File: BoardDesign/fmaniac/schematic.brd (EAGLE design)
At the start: 20 x 39 mm, 20 parts, among them U1 ATMEGA168MLF, X1 STEREOJACK

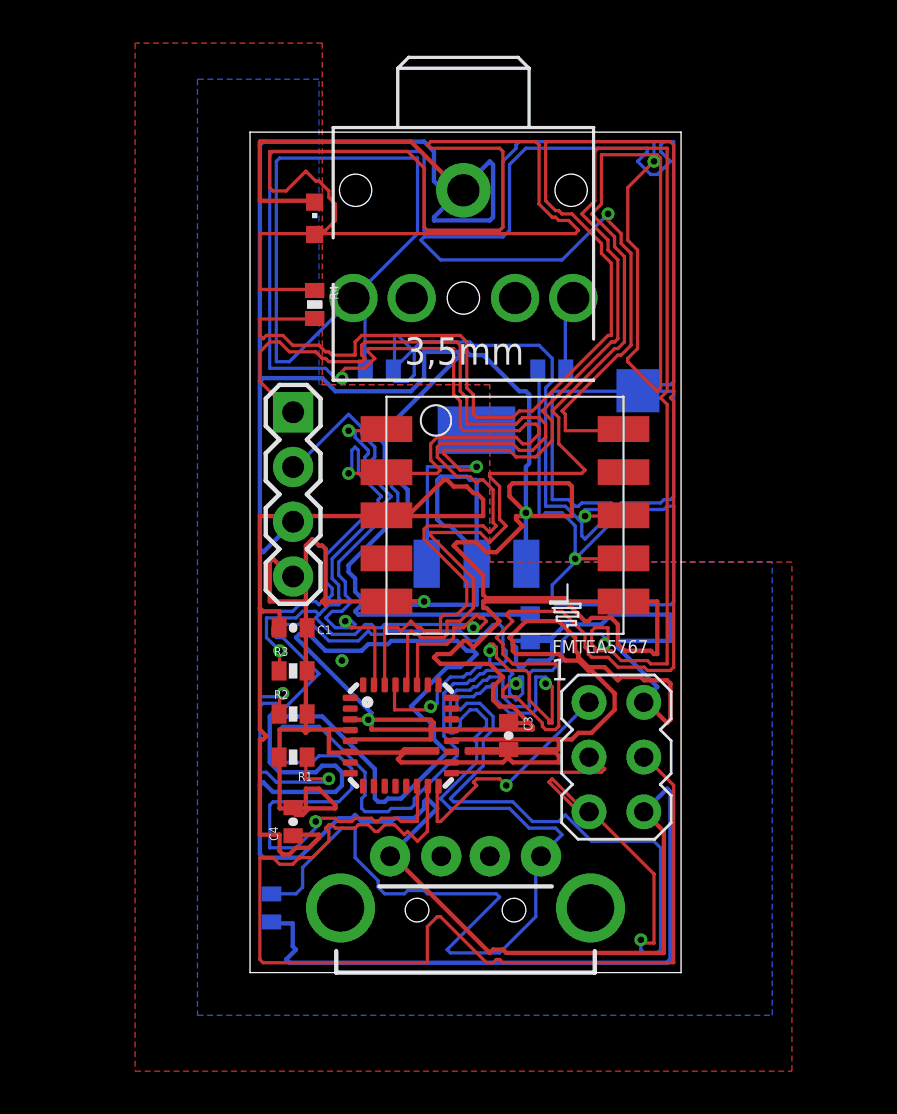
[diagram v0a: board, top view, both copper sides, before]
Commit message: Normal Push, Interrupt Button Added.
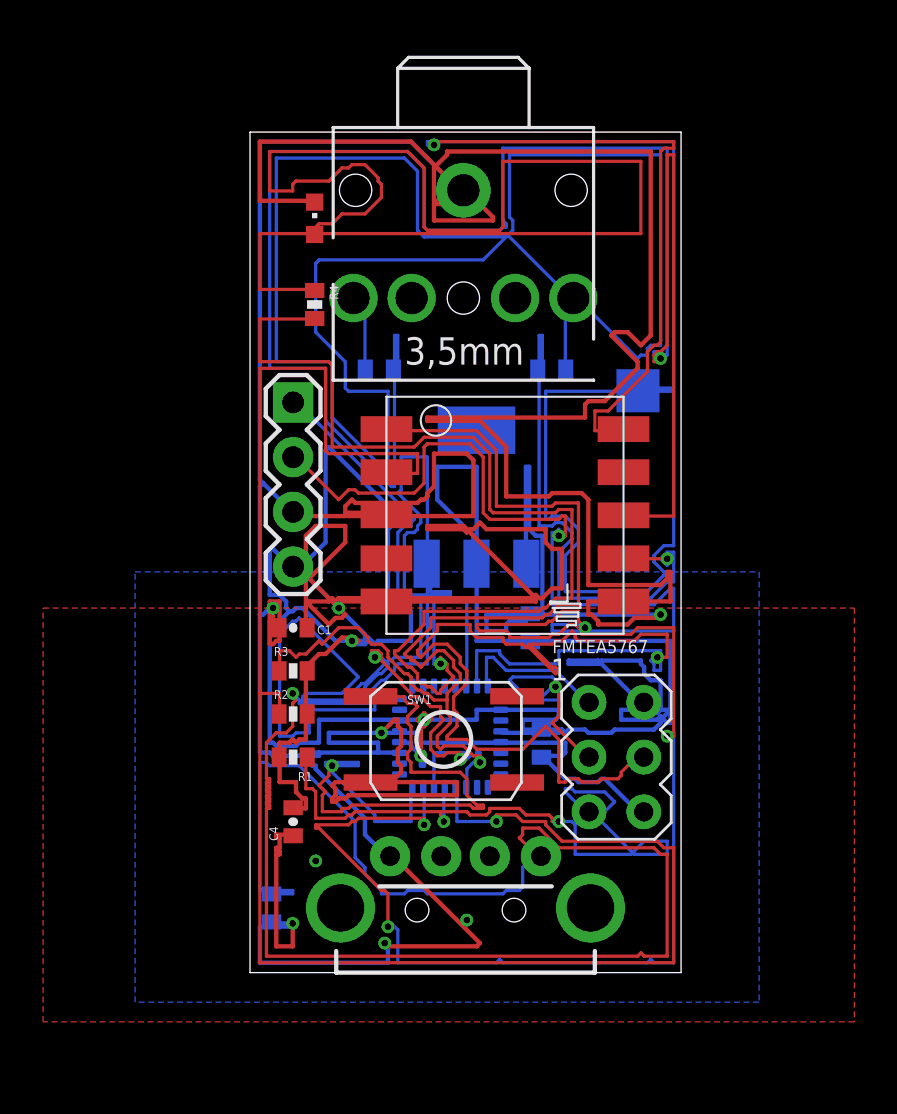
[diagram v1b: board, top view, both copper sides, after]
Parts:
- added SW1: (no value), libraryPart:SWITCH_SMD
- moved U1 2.29 mm to (9.29, 10.9), flipped to the bottom, turned to 180 degrees
- moved C3 1.57 mm to (13.5, 10.6), flipped to the bottom, turned to 90 degrees
- moved UART 0.46 mm to (2.00, 26.5)
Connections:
- new net INT0: SW1.1, U1.32
- net GND: now also SW1.3
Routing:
- net ROUT: track 3.59 -> 86.4 mm
- net SS: track 132.9 -> 54.3 mm, vias 2 -> 1
- net TXD: track 22.8 -> 101.2 mm, vias 1 -> 5
- net SCL: track 150.8 -> 80.4 mm, vias 4 -> 1
- net N$4: track 28.7 -> 94.4 mm
- net RST: track 91.0 -> 33.8 mm, vias 5 -> 2
- net GND: track 323.1 -> 266.8 mm, vias 3 -> 7
- net +3V3: track 130.2 -> 185.1 mm, vias 1 -> 4
- net INT0: track 0.00 -> 30.7 mm, vias 0 -> 1
- net LOUT: track 31.6 -> 3.75 mm
- net SDA: track 34.1 -> 50.2 mm, vias 3 -> 1
- net RXD: track 49.6 -> 41.1 mm, vias 0 -> 2
- net ANT: track 77.4 -> 84.4 mm
- net SCK: track 8.18 -> 12.8 mm, vias 0 -> 1
- net MISO: track 11.6 -> 7.01 mm, vias 1 -> 0
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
